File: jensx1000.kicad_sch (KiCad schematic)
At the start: 0 parts

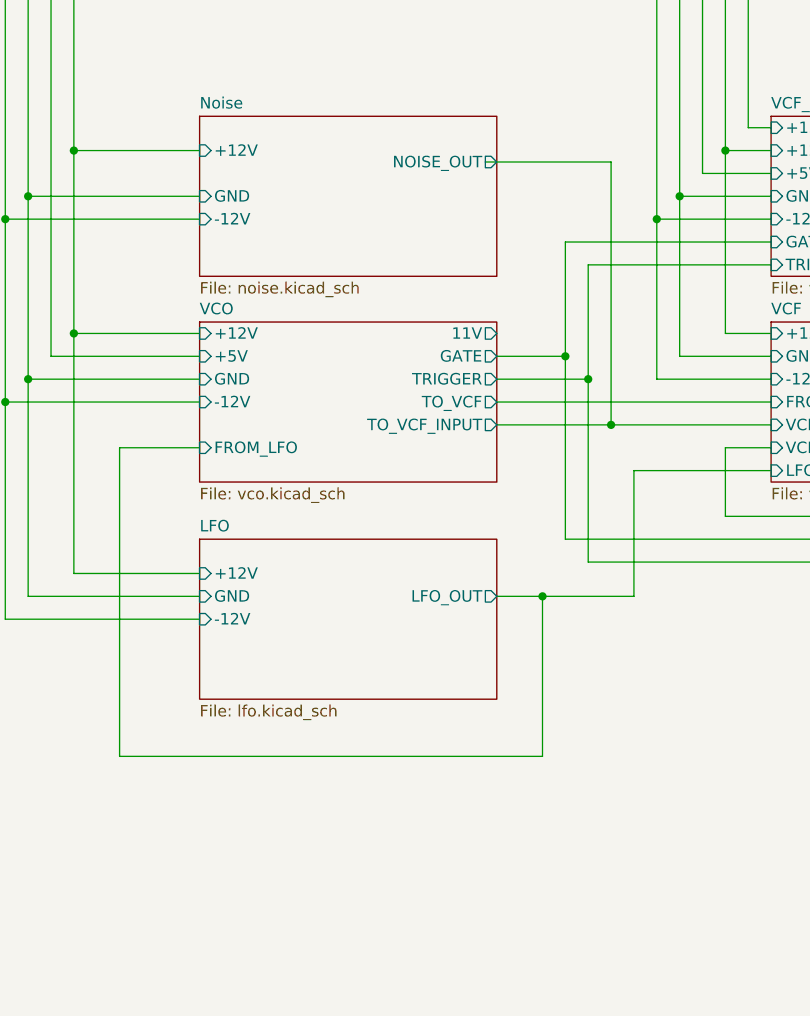
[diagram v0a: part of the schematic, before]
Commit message: Extract keyboard
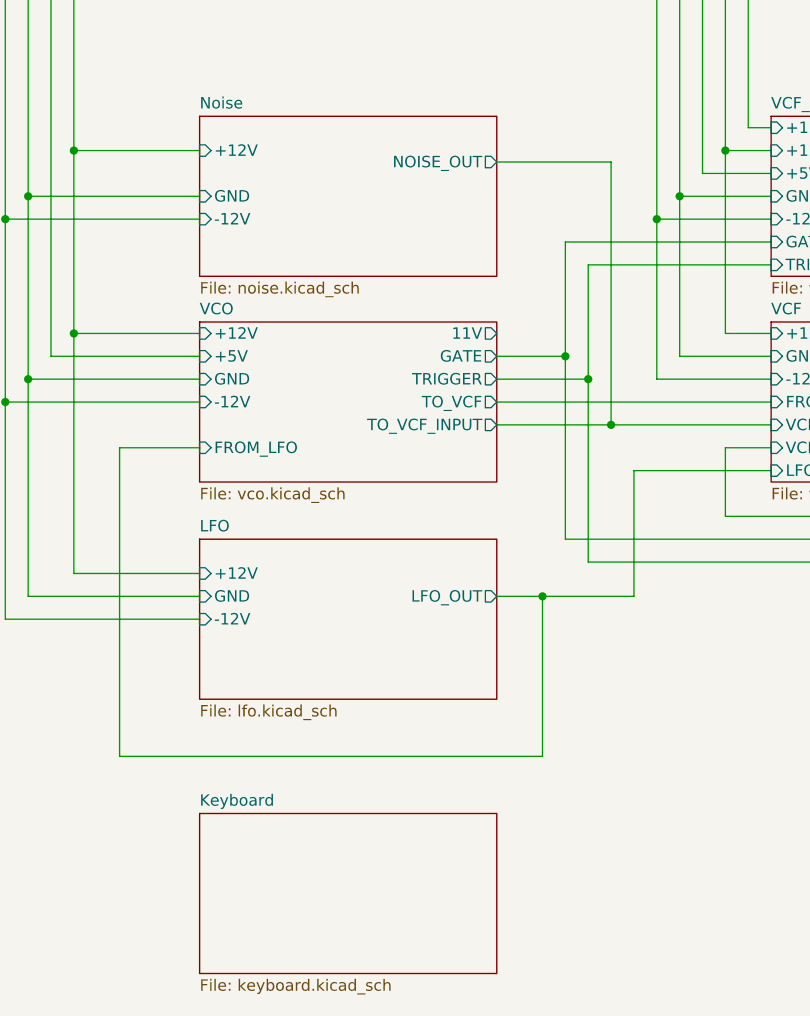
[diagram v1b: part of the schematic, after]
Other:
- added sheet Keyboard (keyboard.kicad_sch)
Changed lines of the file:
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@@
+	(wire
+		(pts
+			(xy 104.14 73.66) (xy 116.84 73.66)
+		)
+		(stroke
+			(width 0)
+			(type default)
+		)
+	)
 	(wire
 		(pts
@@
 		(pts
 			(xy 104.14 102.87) (xy 116.84 102.87)
-		)
-		(stroke
-			(width 0)
-			(type default)
-		)
-	)
-	(wire
-		(pts
-			(xy 102.87 73.66) (xy 116.84 73.66)
 		)
 		(stroke
@@
 				)
 			)
+		)
+	)
+	(sheet
+		(at 71.12 146.05)
+		(size 33.02 17.78)
+		(exclude_from_sim no)
+		(in_bom yes)
+		(on_board yes)
+		(dnp no)
+		(fields_autoplaced yes)
+		(stroke
+			(width 0.1524)
+			(type solid)
+		)
+		(fill
+			(color 0 0 0 0.0000)
+		)
+		(property "Sheetname" "Keyboard"
+			(at 71.12 145.3384 0)
+			(effects
+				(font
+					(size 1.27 1.27)
+				)
+				(justify left bottom)
+			)
+		)
+		(property "Sheetfile" "keyboard.kicad_sch"
+			(at 71.12 164.4146 0)
+			(effects
+				(font
+					(size 1.27 1.27)
+				)
+				(justify left top)
+			)
+		)
+		(instances
+			(project "jensx1000"
+				(path "/3c53febc-5769-4c45-8f8f-0aba2c04e944"
+					(page "10")
+				)
+			)

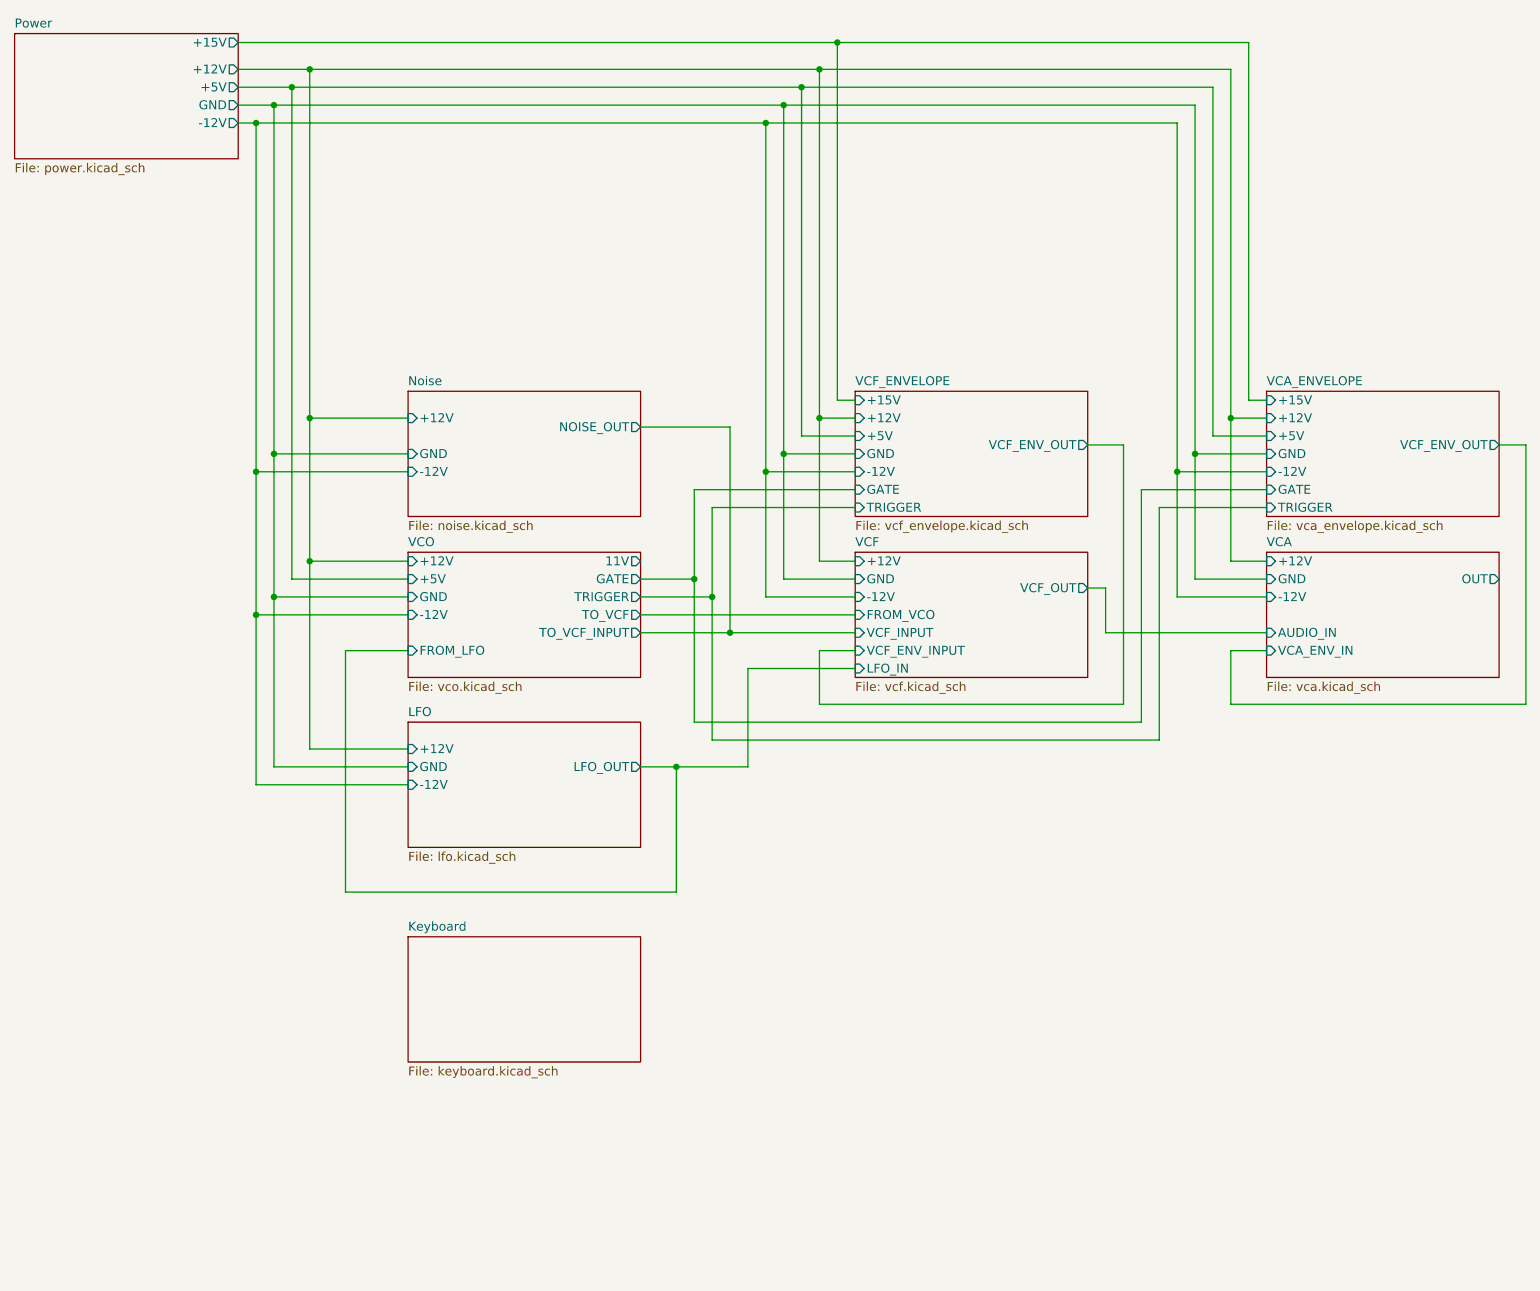
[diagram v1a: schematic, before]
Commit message: Wire up keyboard
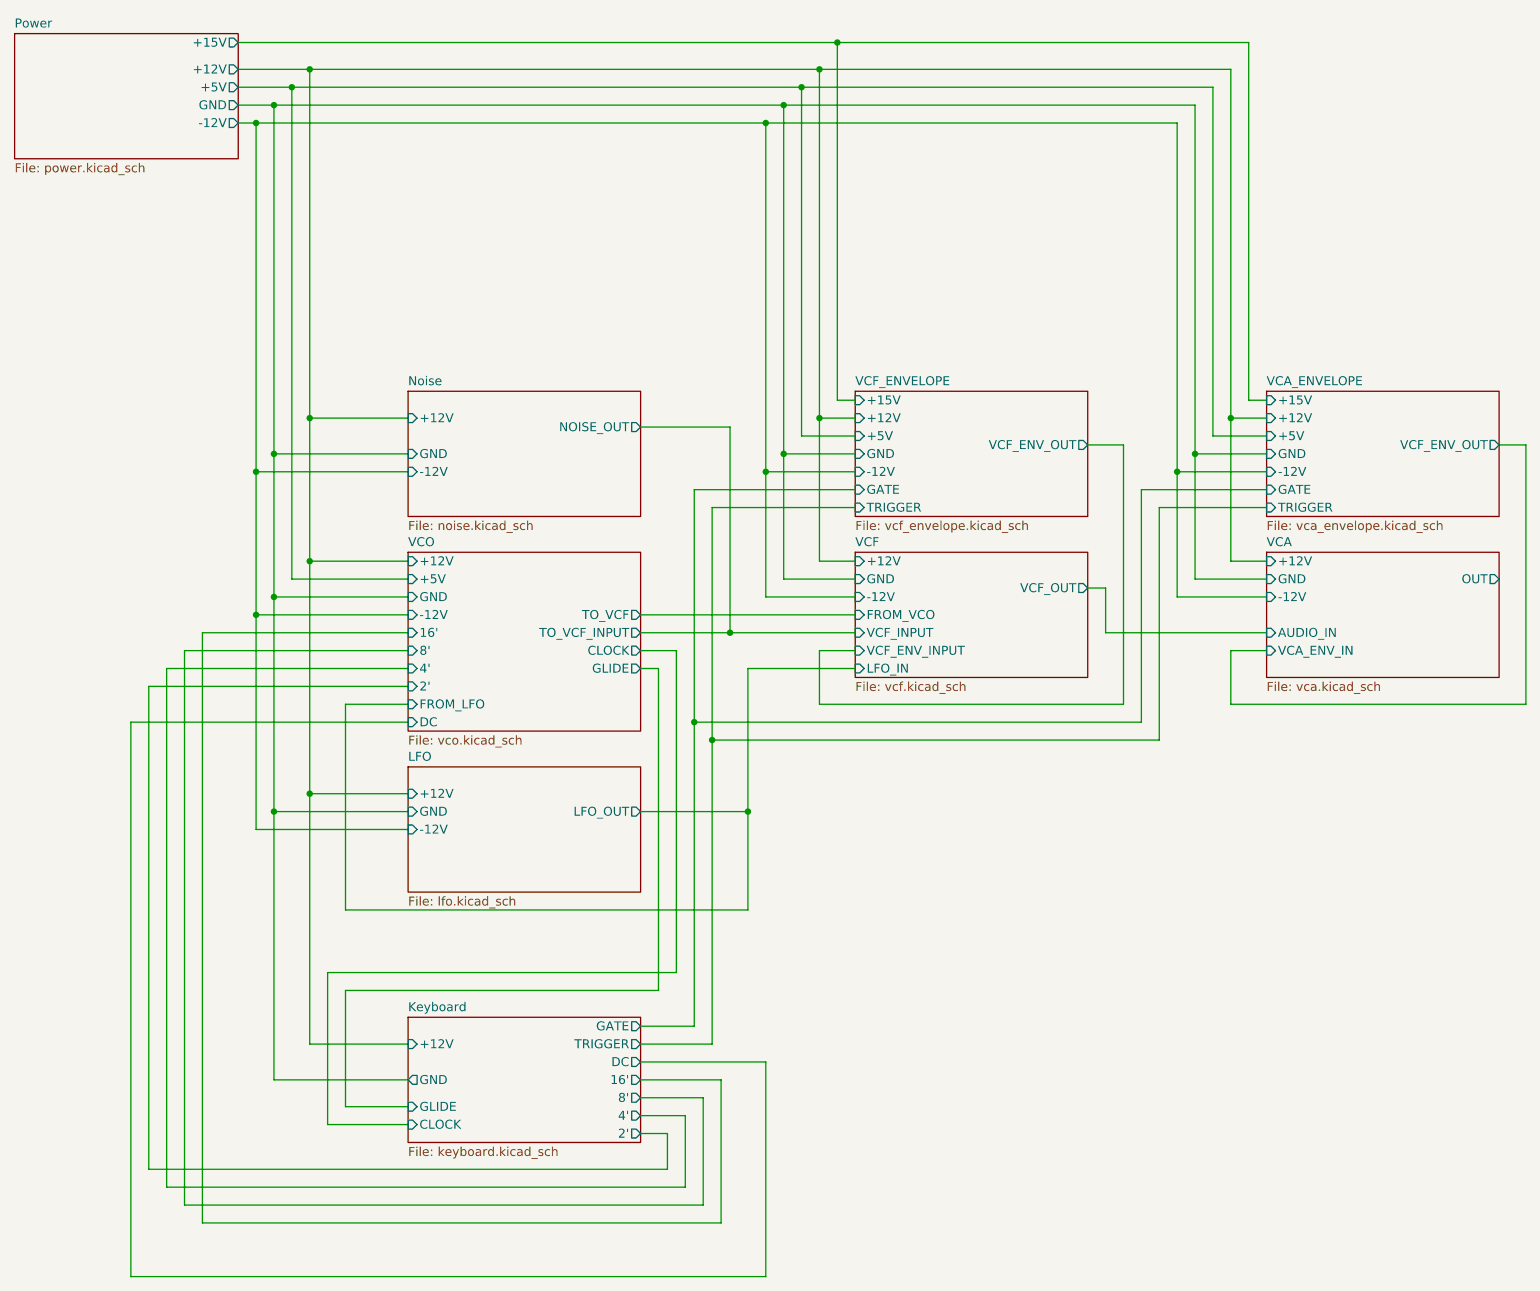
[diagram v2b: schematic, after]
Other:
- sheet Keyboard ports: added +12V, 16', 2', 4', 8', CLOCK, DC, GATE, GLIDE, GND, TRIGGER; removed none
- sheet VCO ports: added 16', 2', 4', 8', CLOCK, DC, GLIDE; removed 11V, GATE, TRIGGER

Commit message: Add missing values and connectors
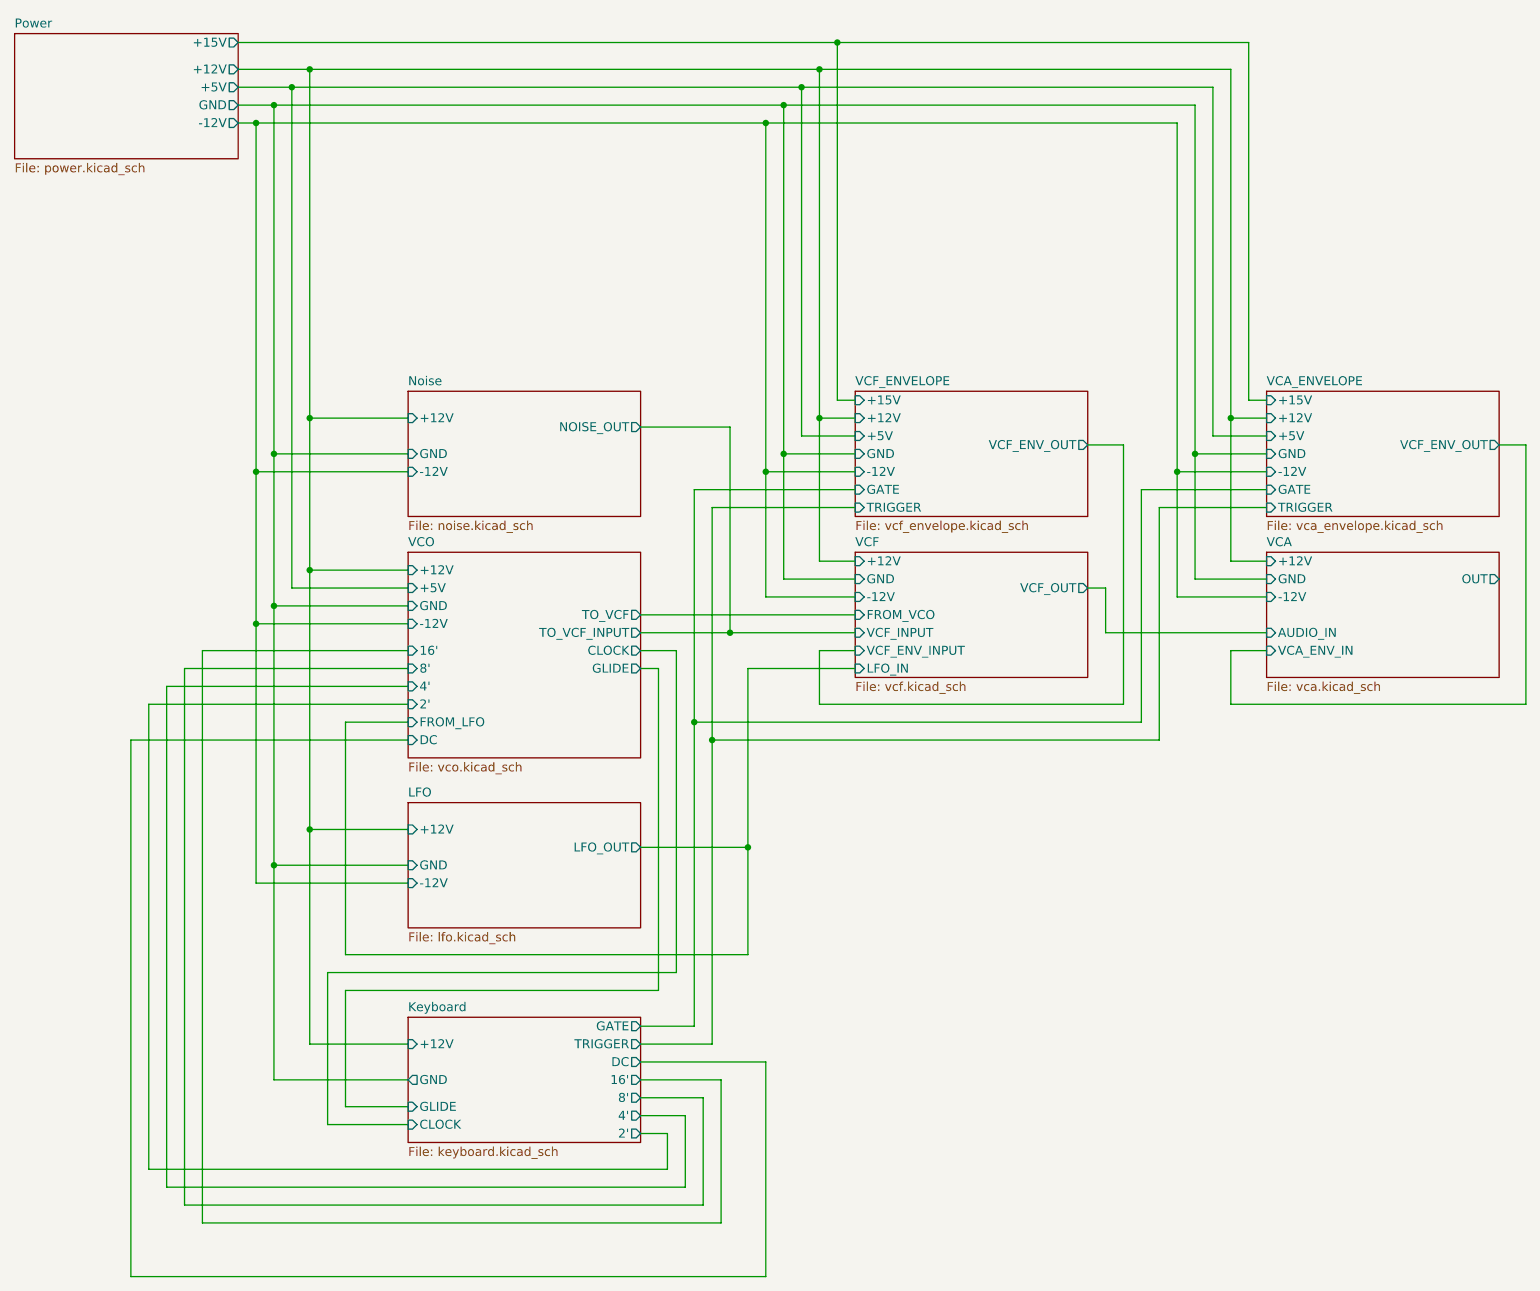
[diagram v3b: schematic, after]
